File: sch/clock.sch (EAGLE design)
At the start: 6 parts, among them IC1 74LS04N, Q1 2N2907

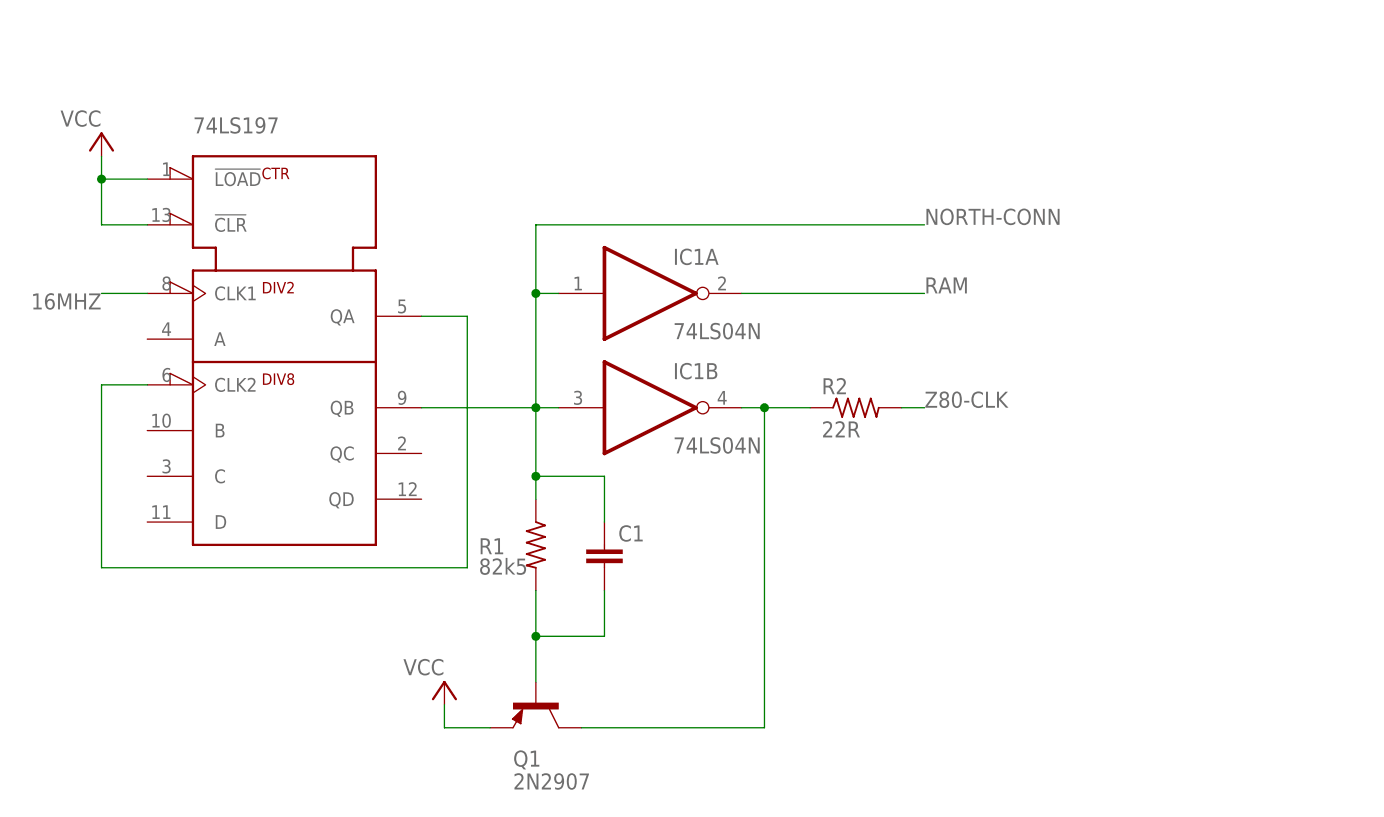
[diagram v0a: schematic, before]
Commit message: Added oscillator to & updated the clock schematic.
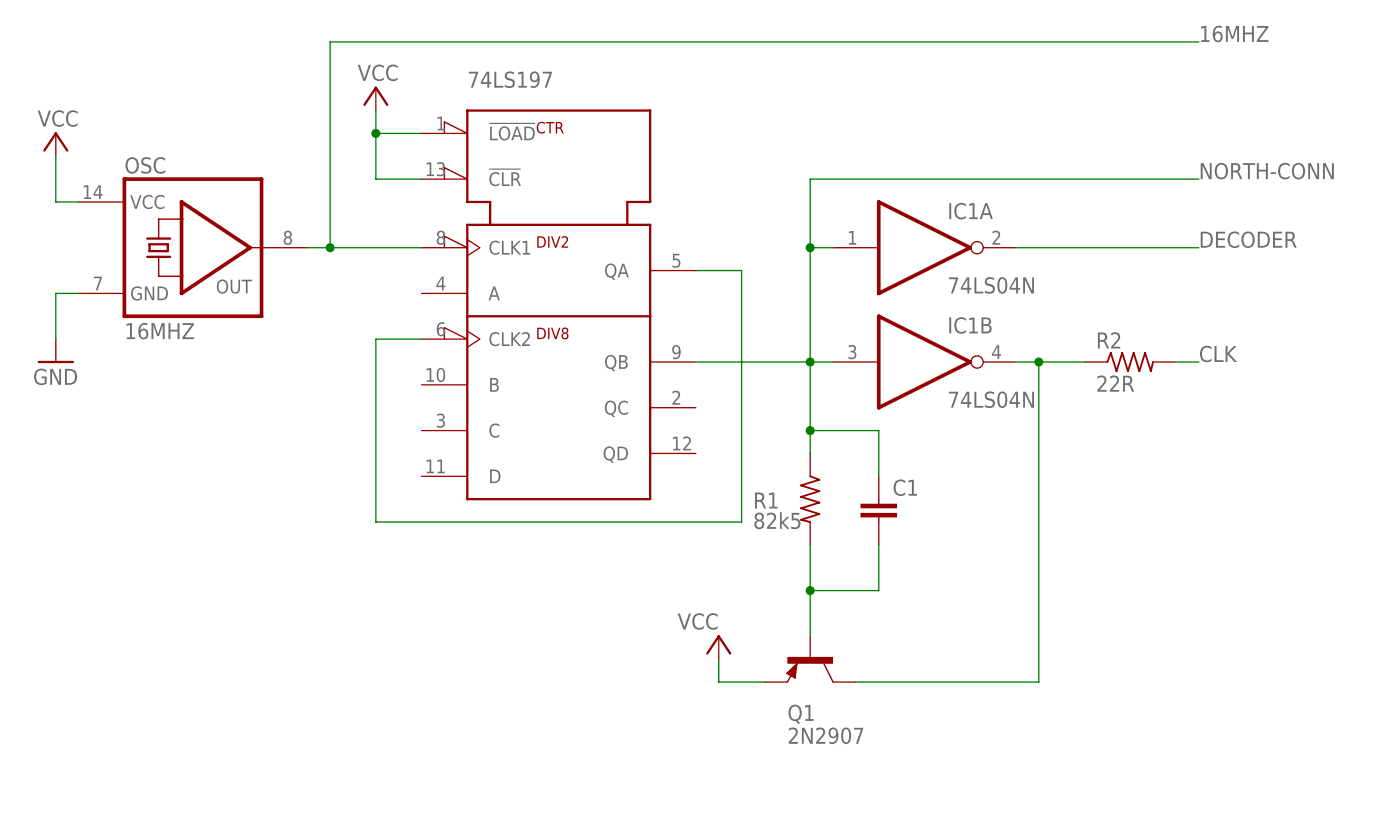
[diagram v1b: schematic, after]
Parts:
- added OSC: 16MHZ, crystal:QG5860
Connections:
- net RAM renamed DECODER
- net Z80-CLK renamed CLK
- new net GND: OSC.GND
- net 16MHZ: now also OSC.OUT
- net VCC: now also OSC.VCC
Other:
- moved on the sheet: C1, IC1A, IC1B, Q1, R1, R2
